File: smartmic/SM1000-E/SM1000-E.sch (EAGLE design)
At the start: 205 parts, among them CN1 HDR100-3, CN10 ST-3509, CN11 HDR100-3, CN12 HRS-A3C-16DA, CN2 JS-MU3-002, CN3 DS-0518, CN4 RJ-45, CN5 ST-3509, CN6 ST-3509, CN7 ST-3509, CN8 ST-3509, CN9 ST-3509, J1 JMP-2PIN, J2 JMP-2PIN, J3 JMP-2PIN, J4 CONN-BOOM-XH-2A, P1 TPAD50, P10 TPAD50, P11 TPAD50, P12 TPAD50, P13 TPAD50, P14 TPAD50, P16 TPAD50, P18 TPAD50, P19 TPAD50, P2 TPAD50, P20 TPAD50, P3 TPAD50, P4 TPAD50, P5 TPAD50, P6 TPAD50, P7 TPAD50, P8 TPAD50, P9 TPAD50, SW1 SW-LC2259, SW2 TS-026, SW3 SW-LC2259EENP, SW4 TS-026, SW5 TS-02B, T1 SM-LP-5001, T2 SM-LP-5001, U1 STM32F405VGT6, U2 LD3985M33R, U3 STMPS2141, U4 EMIF02-USB03F2, U5 TPS54329E, U6 LMV341, U7 LMV341, U8 LM386M-1, U9 LMV341

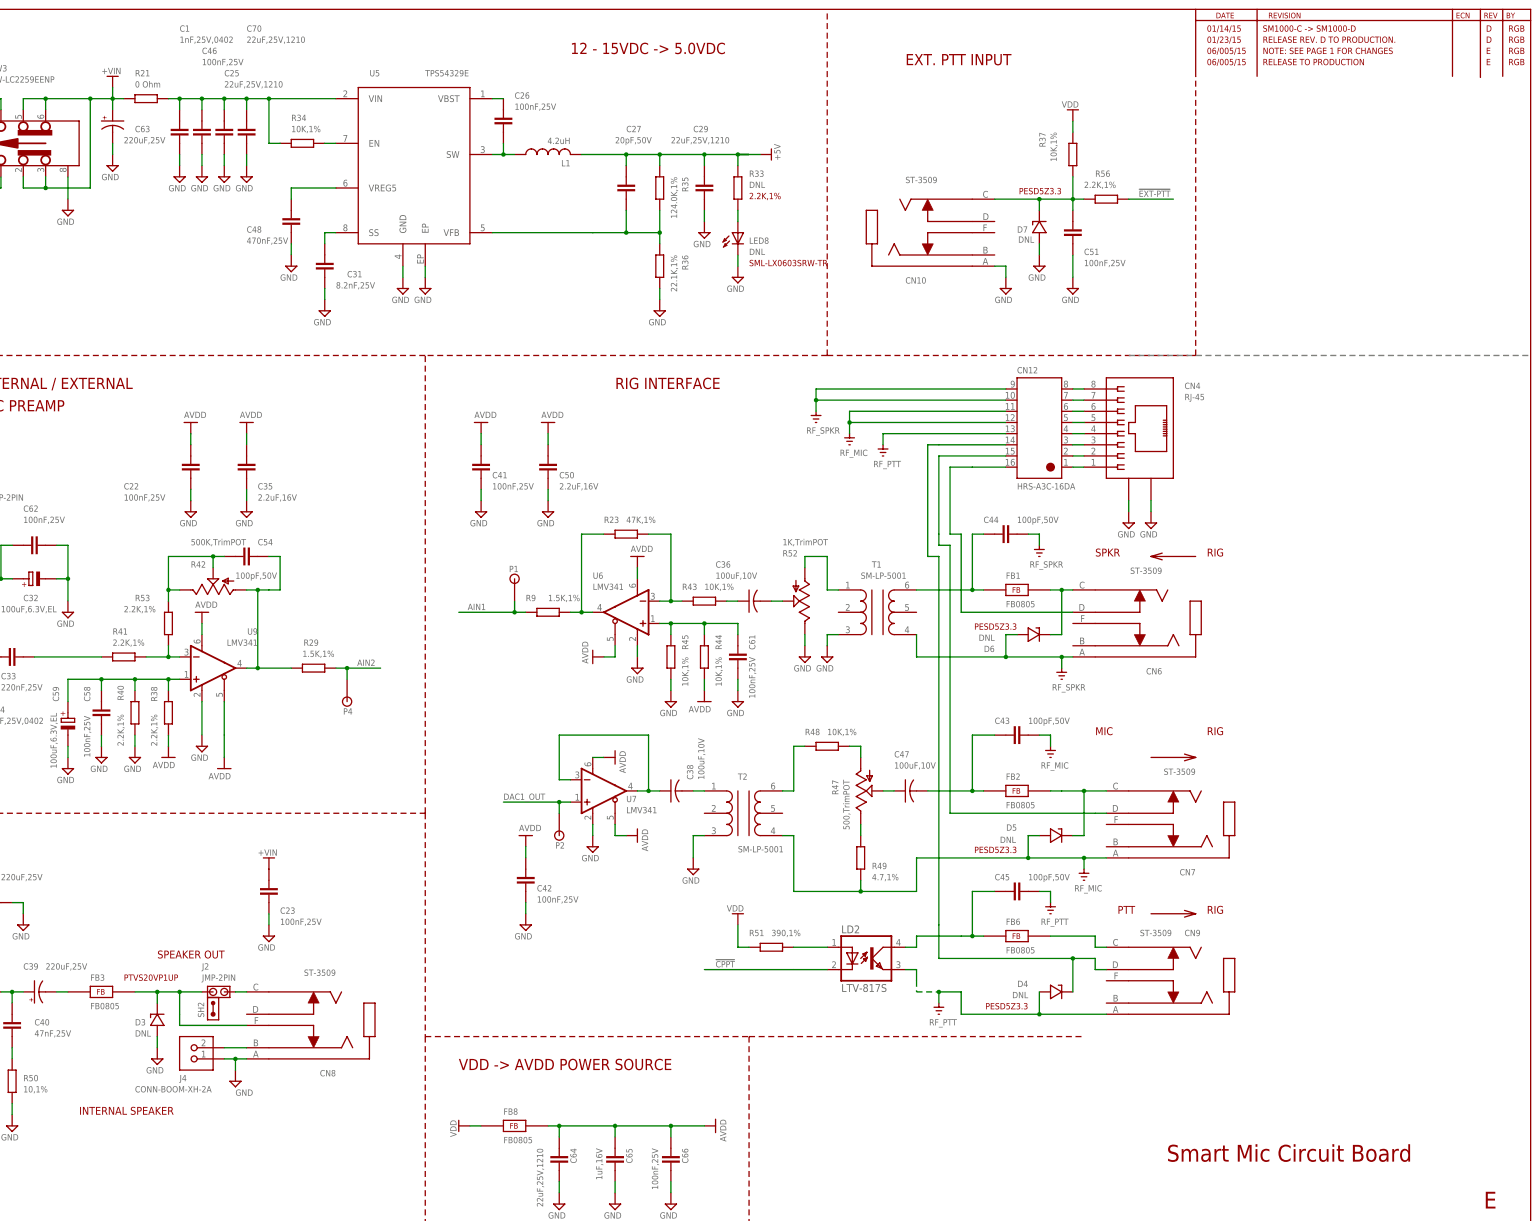
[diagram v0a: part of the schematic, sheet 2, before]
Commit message: UPDATE DESIGN TO FIX PROBLEM WITH SPKR CONN SHORTING AMPLIFIER TO GND WHEN MONO PLUG INSERTED.iNVOLVED CHANGES TO J2 & J4 CONNECTIONS TO CN8. RGB 6/26/15
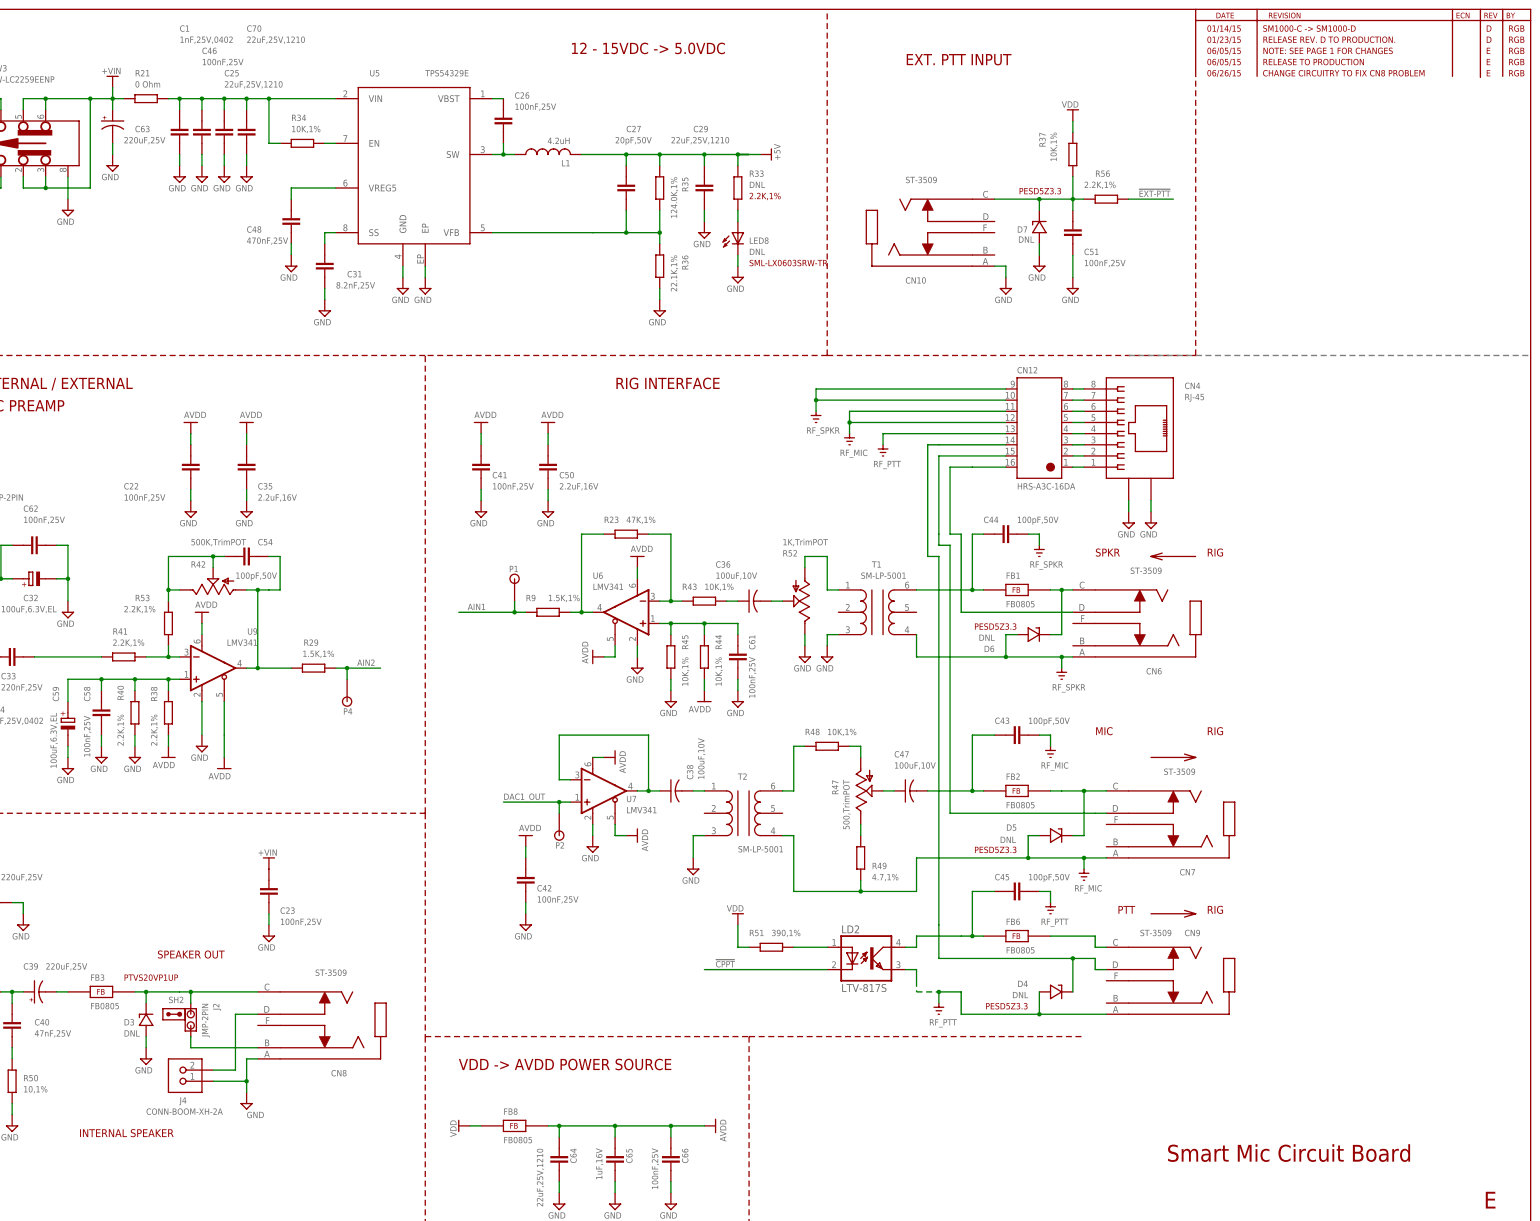
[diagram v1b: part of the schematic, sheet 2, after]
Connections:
- removed net N$75: CN8.C, J2.1
- removed net N$83: CN8.B, J4.2
- new net N$64: CN8.B, J2.1
- new net N$72: CN8.D, J4.2
- net N$62: now also CN8.C; no longer CN8.E
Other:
- note added: "06/26/15"
- note added: "06/27/15"
- note added: "CHANGE CIRCUITRY FOR CN8"
- note added: "CHANGE CIRCUITRY TO FIX CN8 PROBLEM"
- note removed: "06/005/15"
- moved on the sheet: CN8, D3, J2, J4, SH2
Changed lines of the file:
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@@
 <text x="421.64" y="241.3" size="1.4224" layer="94" ratio="10">E</text>
 <text x="426.72" y="241.3" size="1.4224" layer="94" ratio="10">RGB</text>
+<text x="358.14" y="238.76" size="1.4224" layer="94" ratio="10">06/27/15</text>
+<text x="370.84" y="238.76" size="1.4224" layer="94" ratio="10">CHANGE CIRCUITRY FOR CN8</text>
+<text x="421.64" y="238.76" size="1.4224" layer="94" ratio="10">E</text>
+<text x="426.72" y="238.76" size="1.4224" layer="94" ratio="10">RGB</text>
 </plain>
 <instances>
@@
 <text x="10.16" y="144.78" size="1.4224" layer="94" ratio="10">OPT MIC - 2-3</text>
 <text x="287.02" y="266.7" size="2.54" layer="94" ratio="10">EXT. PTT INPUT</text>
-<text x="99.06" y="27.94" size="1.778" layer="94" ratio="10">INTERNAL SPEAKER</text>
+<text x="99.06" y="22.86" size="1.778" layer="94" ratio="10">INTERNAL SPEAKER</text>
 <wire x1="353.06" y1="200.66" x2="353.06" y2="264.16" width="0.1524" layer="94" style="longdash"/>
 <wire x1="337.82" y1="200.66" x2="429.26" y2="200.66" width="0.1524" layer="95" style="longdash"/>
@@
 <text x="109.22" y="58.42" size="1.4224" layer="94" ratio="10">PTVS20VP1UP</text>
 <text x="45.72" y="116.84" size="1.4224" layer="94" ratio="10">PESD5Z3.3</text>
-<text x="355.6" y="269.24" size="1.4224" layer="94" ratio="10">06/005/15</text>
-<text x="355.6" y="266.7" size="1.4224" layer="94" ratio="10">06/005/15</text>
+<text x="355.6" y="269.24" size="1.4224" layer="94" ratio="10">06/05/15</text>
+<text x="355.6" y="266.7" size="1.4224" layer="94" ratio="10">06/05/15</text>
 <text x="368.3" y="266.7" size="1.4224" layer="94" ratio="10">RELEASE TO PRODUCTION</text>
 <text x="419.1" y="266.7" size="1.4224" layer="94" ratio="10">E</text>
@@
 <text x="424.18" y="269.24" size="1.4224" layer="94" ratio="10">RGB</text>
 <text x="424.18" y="266.7" size="1.4224" layer="94" ratio="10">RGB</text>
+<text x="355.6" y="264.16" size="1.4224" layer="94" ratio="10">06/26/15</text>
+<text x="368.3" y="264.16" size="1.4224" layer="94" ratio="10">CHANGE CIRCUITRY TO FIX CN8 PROBLEM</text>
+<text x="419.1" y="264.16" size="1.4224" layer="94" ratio="10">E</text>
+<text x="424.18" y="264.16" size="1.4224" layer="94" ratio="10">RGB</text>
 </plain>
 <instances>
@@
 <attribute name="VALUE" x="81.28" y="22.098" size="1.4224" layer="96" ratio="9"/>
 </instance>
-<instance part="V66" gate="GND" x="134.62" y="35.56" smashed="yes">
-<attribute name="VALUE" x="134.62" y="32.258" size="1.4224" layer="96" ratio="9"/>
+<instance part="V66" gate="GND" x="137.16" y="30.48" smashed="yes">
+<attribute name="VALUE" x="137.16" y="27.178" size="1.4224" layer="96" ratio="9"/>
 </instance>
 <instance part="V67" gate="GND" x="60.96" y="48.26" smashed="yes">
@@
 <instance part="CN6" gate="G$1" x="330.2" y="139.7" rot="R180"/>
 <instance part="CN5" gate="G$1" x="33.02" y="124.46" rot="MR180"/>
-<instance part="CN8" gate="G$1" x="142.24" y="48.26" smashed="yes" rot="R180">
-<attribute name="NAME" x="157.48" y="38.1" size="1.4224" layer="95" ratio="10" rot="R180"/>
-<attribute name="VALUE" x="157.48" y="60.96" size="1.4224" layer="95" ratio="10" rot="R180"/>
+<instance part="CN8" gate="G$1" x="144.78" y="48.26" smashed="yes" rot="R180">
+<attribute name="NAME" x="160.02" y="38.1" size="1.4224" layer="95" ratio="10" rot="R180"/>
+<attribute name="VALUE" x="160.02" y="60.96" size="1.4224" layer="95" ratio="10" rot="R180"/>
 </instance>
 <instance part="CN9" gate="G$1" x="337.82" y="58.42" smashed="yes" rot="R180">
@@
 <attribute name="VALUE" x="78.74" y="264.16" size="1.4224" layer="95" ratio="10" rot="MR180"/>
 </instance>
-<instance part="J4" gate="G$1" x="124.46" y="43.18" smashed="yes" rot="R90">
-<attribute name="NAME" x="121.92" y="35.56" size="1.4224" layer="95" ratio="10"/>
-<attribute name="VALUE" x="111.76" y="33.02" size="1.4224" layer="95" ratio="10"/>
+<instance part="J4" gate="G$1" x="121.92" y="38.1" smashed="yes" rot="R90">
+<attribute name="NAME" x="121.92" y="30.48" size="1.4224" layer="95" ratio="10"/>
+<attribute name="VALUE" x="114.3" y="27.94" size="1.4224" layer="95" ratio="10"/>
 </instance>
 <instance part="V121" gate="GND" x="96.52" y="233.68" smashed="yes">
@@
 <attribute name="VALUE" x="73.66" y="230.378" size="1.4224" layer="96" ratio="9"/>
 </instance>
-<instance part="J2" gate="G$1" x="132.08" y="55.88" smashed="yes" rot="R180">
-<attribute name="NAME" x="127" y="60.96" size="1.4224" layer="95"/>
-<attribute name="VALUE" x="127" y="58.42" size="1.4224" layer="96" ratio="9"/>
+<instance part="J2" gate="G$1" x="124.46" y="48.26" smashed="yes" rot="R90">
+<attribute name="NAME" x="129.54" y="53.34" size="1.4224" layer="95" rot="R270"/>
+<attribute name="VALUE" x="127" y="53.34" size="1.4224" layer="96" ratio="9" rot="R270"/>
 </instance>
-<instance part="SH2" gate="G$1" x="129.54" y="50.8" smashed="yes" rot="R90">
-<attribute name="NAME" x="127.508" y="50.038" size="1.4224" layer="95" ratio="9" rot="R90"/>
+<instance part="SH2" gate="G$1" x="121.92" y="50.8" smashed="yes" rot="R180">
+<attribute name="NAME" x="119.38" y="53.34" size="1.4224" layer="95" ratio="9"/>
 </instance>
 <instance part="D1" gate="G$1" x="33.02" y="251.46" smashed="yes" rot="R90">
@@
 <attribute name="VALUE" x="30.48" y="240.538" size="1.4224" layer="96" ratio="9"/>
 </instance>
-<instance part="D3" gate="G$1" x="116.84" y="48.26" smashed="yes" rot="R90">
-<attribute name="NAME" x="111.76" y="48.26" size="1.4224" layer="95" ratio="10"/>
-<attribute name="VALUE" x="111.76" y="45.72" size="1.4224" layer="96" ratio="10"/>
+<instance part="D3" gate="G$1" x="114.3" y="48.26" smashed="yes" rot="R90">
+<attribute name="NAME" x="109.22" y="48.26" size="1.4224" layer="95" ratio="10"/>
+<attribute name="VALUE" x="109.22" y="45.72" size="1.4224" layer="96" ratio="10"/>
 </instance>
-<instance part="V142" gate="GND" x="116.84" y="40.64" smashed="yes">
-<attribute name="VALUE" x="114.3" y="37.338" size="1.4224" layer="96" ratio="9"/>
+<instance part="V142" gate="GND" x="114.3" y="40.64" smashed="yes">
+<attribute name="VALUE" x="111.76" y="37.338" size="1.4224" layer="96" ratio="9"/>
 </instance>
 <instance part="D4" gate="G$1" x="320.04" y="55.88" smashed="yes">
@@
 </segment>
 <segment>
-<wire x1="137.16" y1="40.64" x2="134.62" y2="40.64" width="0.1524" layer="91"/>
-<wire x1="134.62" y1="40.64" x2="134.62" y2="38.1" width="0.1524" layer="91"/>
+<wire x1="139.7" y1="40.64" x2="137.16" y2="40.64" width="0.1524" layer="91"/>
+<wire x1="137.16" y1="40.64" x2="137.16" y2="35.56" width="0.1524" layer="91"/>
 <pinref part="V66" gate="GND" pin="GND"/>
 <pinref part="CN8" gate="G$1" pin="A"/>
+<junction x="137.16" y="35.56"/>
+<wire x1="137.16" y1="35.56" x2="137.16" y2="33.02" width="0.1524" layer="91"/>
 <pinref part="J4" gate="G$1" pin="1"/>
-<wire x1="132.08" y1="40.64" x2="134.62" y2="40.64" width="0.1524" layer="91"/>
-<junction x="134.62" y="40.64"/>
+<wire x1="129.54" y1="35.56" x2="137.16" y2="35.56" width="0.1524" layer="91"/>
 </segment>
 <segment>
@@
 <segment>
 <pinref part="D3" gate="G$1" pin="A"/>
-<wire x1="116.84" y1="45.72" x2="116.84" y2="43.18" width="0.1524" layer="91"/>
+<wire x1="114.3" y1="45.72" x2="114.3" y2="43.18" width="0.1524" layer="91"/>
 <pinref part="V142" gate="GND" pin="GND"/>
 </segment>
@@
 <net name="N$62" class="0">
 <segment>
-<wire x1="121.92" y1="50.8" x2="121.92" y2="48.26" width="0.1524" layer="91"/>
 <pinref part="FB3" gate="G$1" pin="2"/>
-<wire x1="111.76" y1="55.88" x2="116.84" y2="55.88" width="0.1524" layer="91"/>
-<wire x1="116.84" y1="55.88" x2="121.92" y2="55.88" width="0.1524" layer="91"/>
-<wire x1="121.92" y1="50.8" x2="121.92" y2="55.88" width="0.1524" layer="91"/>
-<pinref part="CN8" gate="G$1" pin="E"/>
-<wire x1="137.16" y1="48.26" x2="121.92" y2="48.26" width="0.1524" layer="91"/>
-<pinref part="J2" gate="G$1" pin="2"/>
-<wire x1="121.92" y1="55.88" x2="127" y2="55.88" width="0.1524" layer="91"/>
-<junction x="121.92" y="55.88"/>
+<wire x1="111.76" y1="55.88" x2="114.3" y2="55.88" width="0.1524" layer="91"/>
+<wire x1="114.3" y1="55.88" x2="121.92" y2="55.88" width="0.1524" layer="91"/>
 <pinref part="D3" gate="G$1" pin="C"/>
-<wire x1="116.84" y1="53.34" x2="116.84" y2="55.88" width="0.1524" layer="91"/>
-<junction x="116.84" y="55.88"/>
+<wire x1="114.3" y1="53.34" x2="114.3" y2="55.88" width="0.1524" layer="91"/>
+<junction x="114.3" y="55.88"/>
+<pinref part="CN8" gate="G$1" pin="C"/>
+<wire x1="121.92" y1="55.88" x2="124.46" y2="55.88" width="0.1524" layer="91"/>
+<pinref part="J2" gate="G$1" pin="2"/>
+<wire x1="124.46" y1="55.88" x2="139.7" y2="55.88" width="0.1524" layer="91"/>
+<wire x1="124.46" y1="55.88" x2="124.46" y2="53.34" width="0.1524" layer="91"/>
+<junction x="124.46" y="55.88"/>
 </segment>
 </net>
@@
 </segment>
 </net>
-<net name="N$75" class="0">
-<segment>
-<pinref part="J2" gate="G$1" pin="1"/>
-<pinref part="CN8" gate="G$1" pin="C"/>
-<wire x1="134.62" y1="55.88" x2="137.16" y2="55.88" width="0.1524" layer="91"/>
-</segment>
-</net>
-<net name="N$83" class="0">
-<segment>
-<pinref part="J4" gate="G$1" pin="2"/>
-<pinref part="CN8" gate="G$1" pin="B"/>
-<wire x1="132.08" y1="43.18" x2="137.16" y2="43.18" width="0.1524" layer="91"/>
-</segment>
-</net>
 <net name="N$84" class="0">
 <segment>
@@
 </segment>
 </net>
+<net name="N$64" class="0">
+<segment>
+<pinref part="J2" gate="G$1" pin="1"/>
+<wire x1="124.46" y1="45.72" x2="124.46" y2="43.18" width="0.1524" layer="91"/>
+<pinref part="CN8" gate="G$1" pin="B"/>
+<wire x1="124.46" y1="43.18" x2="139.7" y2="43.18" width="0.1524" layer="91"/>
+</segment>
+</net>
+<net name="N$72" class="0">
+<segment>
+<pinref part="CN8" gate="G$1" pin="D"/>
+<wire x1="139.7" y1="50.8" x2="134.62" y2="50.8" width="0.1524" layer="91"/>
+<wire x1="134.62" y1="50.8" x2="134.62" y2="38.1" width="0.1524" layer="91"/>
+<wire x1="134.62" y1="38.1" x2="129.54" y2="38.1" width="0.1524" layer="91"/>
+<pinref part="J4" gate="G$1" pin="2"/>
+</segment>
+</net>
